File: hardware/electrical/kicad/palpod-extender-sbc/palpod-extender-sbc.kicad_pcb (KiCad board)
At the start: 8 copper layers, 100 x 100 mm, 0 parts

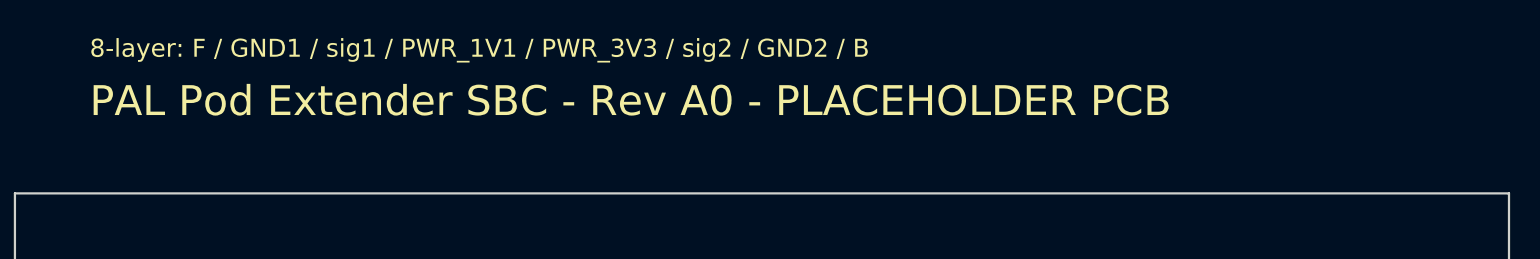
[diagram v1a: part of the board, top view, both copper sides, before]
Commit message: brand: broad KiCad sweep — remaining PAL Pod strings → Hearth
Targeted-pattern sed in ff14a48 missed variants. Broad find-replace
on .kicad_sch/pcb/pro/sym/mod + fp-lib-table + sym-lib-table +
per-project README.md (only where PAL Pod string actually appeared).
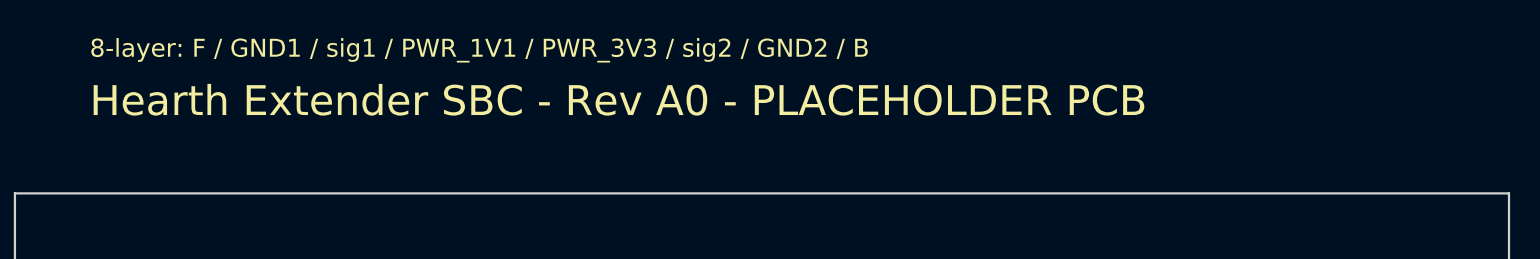
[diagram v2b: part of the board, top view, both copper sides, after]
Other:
- board text added: "Hearth Extender SBC - Rev A0 - PLACEHOLDER PCB"
- board text removed: "PAL Pod Extender SBC - Rev A0 - PLACEHOLDER PCB"
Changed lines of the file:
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@@
   (paper "A3")
   (title_block
-    (title "PAL Pod Extender SBC - PCB")
+    (title "Hearth Extender SBC - PCB")
     (date "2026-08-03")
     (rev "A0")
@@
   (gr_line (start 0 100) (end 0 0)
     (stroke (width 0.15) (type solid)) (layer "Edge.Cuts") (uuid "edge0004"))
-  (gr_text "PAL Pod Extender SBC - Rev A0 - PLACEHOLDER PCB"
+  (gr_text "Hearth Extender SBC - Rev A0 - PLACEHOLDER PCB"
     (at 5 -5 0) (layer "F.SilkS") (uuid "silk0001")
     (effects (font (size 2 2) (thickness 0.3)) (justify left bottom)))
